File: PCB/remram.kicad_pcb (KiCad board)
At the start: 4 copper layers, 140 x 104 mm, 255 parts, among them J1 4DB-P108-06, J10 Conn_02x13_Odd_Even, J11 70543-0001, J12 70543-0002, J13 70543-0002, J14 70543-0002, J15 70543-0001, J16 70543-0002, J17 70543-0002, J18 70543-0002, J19 70543-0001, J2 039531-1002, J20 70543-0003, J21 70543-0003, J22 70543-0003, J23 70543-0003, J3 70543-0003, J4 67068-8000, J5 Conn_02x05, J6 Conn_02x05, J7 70543-0002, J8 70543-0002, J9 62201021121, Q1 PSMN1R2-30YLC,115, Q2 BUK9840-55, Q3 PSMN1R2-30YLC,115, Q4 BUK9840-55, Q5 IRLML6401, SW1 OS102011MA1QN1, SW2 PTS645VL39-2, U1 TPS54308, U2 AP2112K-3.3TRG1, U3 ADUM4160, U4 STM32F765VIT6, U5 TMC2130-TA, U6 TMC2130-TA, U7 TMC2130-TA, U8 TMC2130-TA, U9 SN74LVC2G17DCKR, Y1 TSX-3225 24.0000MF15X-AC3

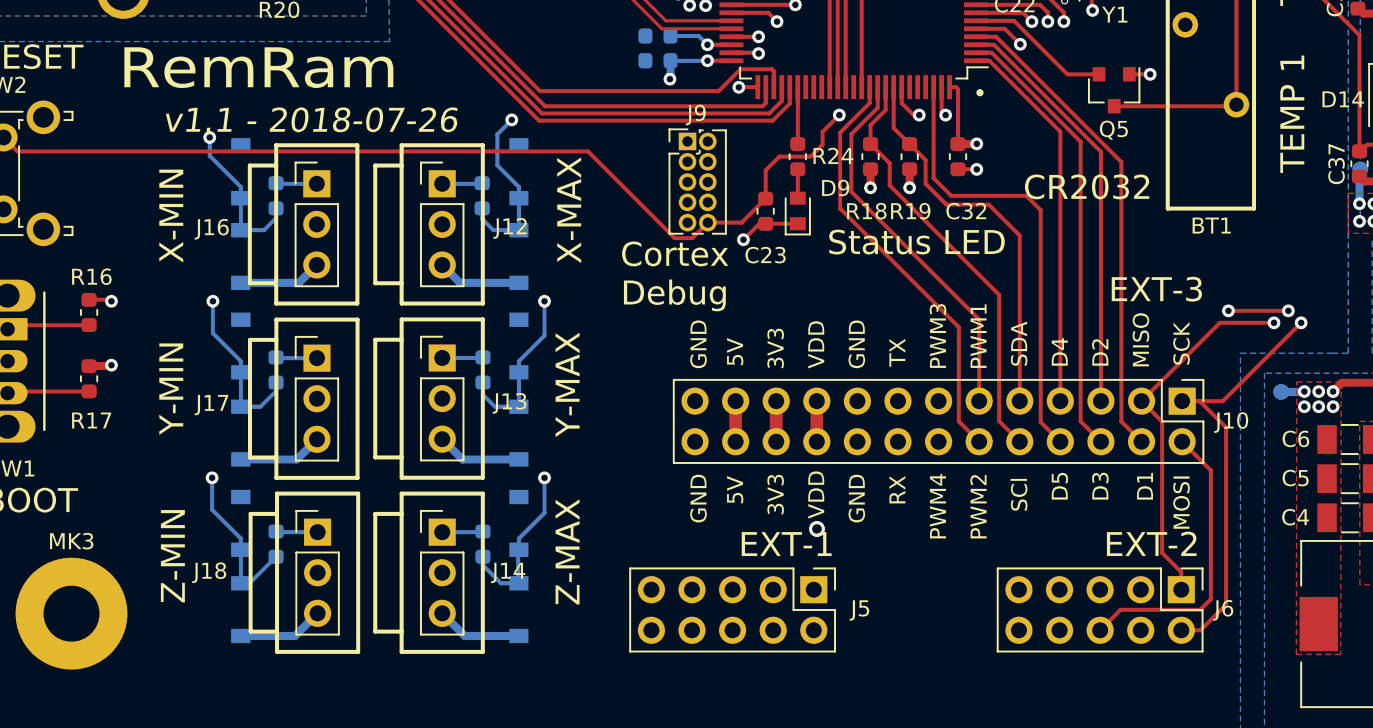
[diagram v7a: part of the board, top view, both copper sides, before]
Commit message: Add series resistors to EXT-2 SPI lines
To help with noisy ribbon cables and SD card communication we
add three 100 ohm resistors in series for the SPI pins.
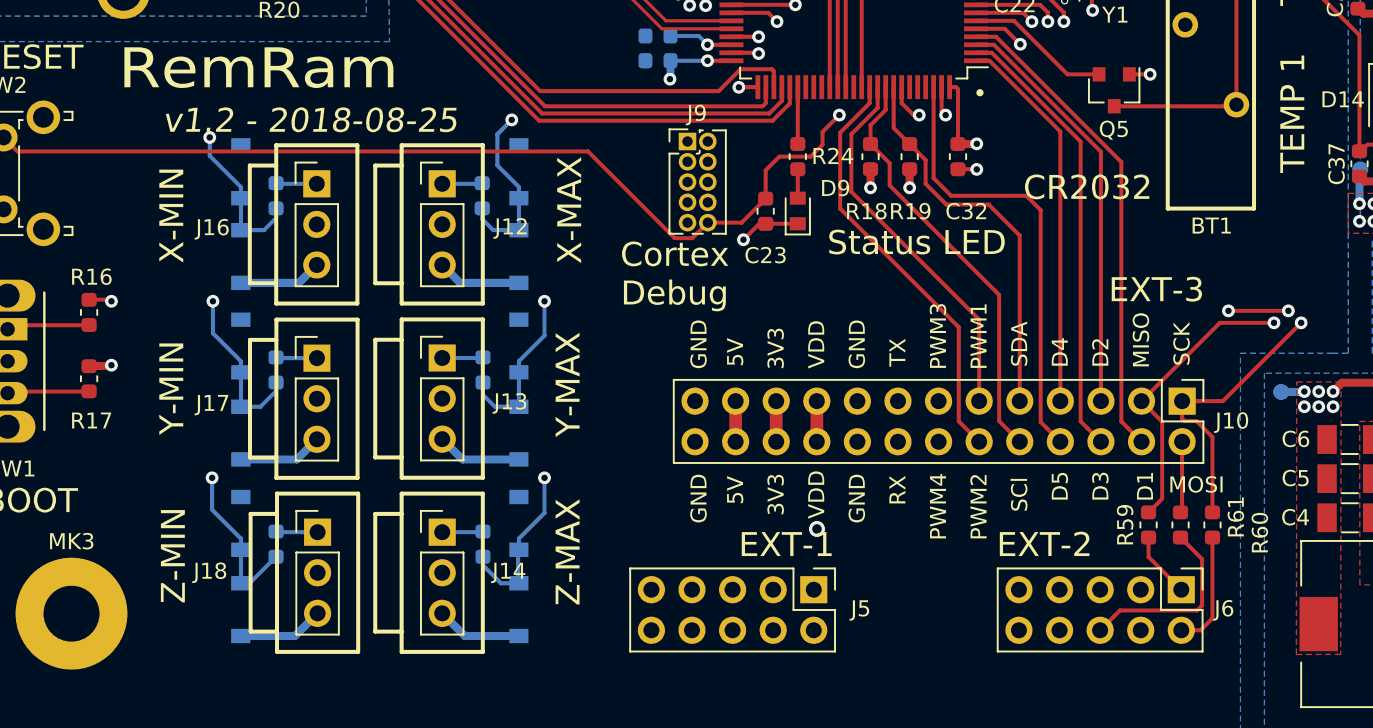
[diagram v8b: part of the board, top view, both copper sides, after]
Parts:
- added R59: 100, Resistor_SMD:R_0603_1608Metric, F.Cu at (136.7, 132.0)
- added R60: 100, Resistor_SMD:R_0603_1608Metric, F.Cu at (140.7, 132.0)
- added R61: 100, Resistor_SMD:R_0603_1608Metric, F.Cu at (138.7, 132.0)
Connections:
- J6 pad 1: /MCU/MISO -> Net-(J6-Pad1)
- J6 pad 2: /MCU/SCK -> Net-(J6-Pad2)
- J6 pad 6: /MCU/MOSI -> Net-(J6-Pad6)
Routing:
- net /MCU/MOSI: track 177.2 -> 163.4 mm
- net Net-(J6-Pad6): track 0.00 -> 11.8 mm
- net /MCU/SCK: track 173.9 -> 165.2 mm
- net Net-(J6-Pad2): track 0.00 -> 7.37 mm
- net /MCU/MISO: track 168.9 -> 163.9 mm
- net Net-(J6-Pad1): track 0.00 -> 4.11 mm
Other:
- board text added: "v1.2 - 2018-08-25"
- board text removed: "v1.1 - 2018-07-26"
